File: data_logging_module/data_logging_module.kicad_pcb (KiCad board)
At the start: 2 copper layers, 40 parts, among them U1 PCF8563TS, U2 TLV62569DBV, U3 BME280, Y1 32768Hz

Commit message: Initial scheme
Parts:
- removed D9: D, Diode_SMD:D_PowerDI-123
- added C104: 22u, Capacitor_SMD:C_0805_2012Metric, F.Cu at (205.9, 80.5)
- added C105: 22u, Capacitor_SMD:C_0805_2012Metric, F.Cu at (205.9, 83.5)
- added C301: 100nF, Capacitor_SMD:C_0805_2012Metric, F.Cu at (205.7, 56.0)
- added C302: 100nF, Capacitor_SMD:C_0805_2012Metric, F.Cu at (205.7, 59.0)
- added C303: 100nF, Capacitor_SMD:C_0805_2012Metric, F.Cu at (205.7, 62.1)
- added C304: 100nF, Capacitor_SMD:C_0805_2012Metric, F.Cu at (205.7, 65.1)
- added D201: PESD3V3L1BA,115, Diode_SMD:D_SOD-323, F.Cu at (194.8, 59.0)
- added D202: PESD3V3L1BA,115, Diode_SMD:D_SOD-323, F.Cu at (194.8, 56.0)
- added J1: Conn_01x11, Connector_PinHeader_2.54mm:PinHeader_1x11_P2.54mm_Vertical, F.Cu at (238.6, 57.6)
- added J2: Conn_01x11, Connector_PinHeader_2.54mm:PinHeader_1x11_P2.54mm_Vertical, F.Cu at (243.2, 57.6)
- added R107: 10R, Resistor_SMD:R_0805_2012Metric, F.Cu at (210.3, 80.5)
- added R200: 10kR, Resistor_SMD:R_0805_2012Metric, F.Cu at (194.8, 64.9)
- added R201: 10kR, Resistor_SMD:R_0805_2012Metric, F.Cu at (194.8, 61.9)
- added R301: 4k7R, Resistor_SMD:R_0805_2012Metric, F.Cu at (201.2, 67.8)
- added R302: 4k7R, Resistor_SMD:R_0805_2012Metric, F.Cu at (201.2, 64.9)
- added R303: 4k7R, Resistor_SMD:R_0805_2012Metric, F.Cu at (201.2, 61.9)
- added R304: 5k1R, Resistor_SMD:R_0805_2012Metric, F.Cu at (201.2, 56.0)
- added R305: 5k1R, Resistor_SMD:R_0805_2012Metric, F.Cu at (201.2, 59.0)
- added U101: HT7533-1, Package_TO_SOT_SMD:SOT-89-3, F.Cu at (207.1, 76.0)
- added U301: BME280, Package_LGA:Bosch_LGA-8_2.5x2.5mm_P0.65mm_ClockwisePinNumbering, F.Cu at (205.7, 68.8)
- added U5: DS18B20, Package_TO_SOT_THT:TO-92_Inline, F.Cu at (209.9, 67.5)
- RLO300: renamed from R10; value LDR07 -> LDR
- renumbered C6 to C100, C7 to C101, C8 to C102, C9 to C103, C10 to C106, C4 to C200, C5 to C201, C11 to C300, C2 to C400, C3 to C401, C1 to C402, D10 to D100, D3 to D200, D4 to D203, D5 to D204, D6 to D205, D7 to D206, D1 to D400, D2 to D401, L1 to L100, R7 to R104, R8 to R105, R9 to R106, R3 to R202, R4 to R203, R5 to R204, R6 to R205, R11 to R300, R1 to R400, R2 to R401, U2 to U100, U3 to U300, U1 to U400, Y1 to Y400
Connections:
- net LDR_IN renamed LDR
- net SD_CARD_CS renamed SD_CARD_CS/DAT3
- net SD_CARD_MISO renamed SD_CARD_DAT2
- net SD_CARD_MOSI renamed SD_CARD_DAT1
- net SD_CARD_SCK renamed SD_CARD_DAT0/MISO
- RLO300 pad 2: +3.3V -> +3.3VA
- U300 pad 1: unconnected-(U3-GND-Pad1) -> GND
- U300 pad 2: unconnected-(U3-CSB-Pad2) -> +3.3V
- U300 pad 3: unconnected-(U3-SDI-Pad3) -> I2C_SDA
- U300 pad 4: unconnected-(U3-SCK-Pad4) -> I2C_SCL
- U300 pad 5: unconnected-(U3-SDO-Pad5) -> Net-(U300-SDO)
- U300 pad 6: unconnected-(U3-VDDIO-Pad6) -> +3.3V
- U300 pad 7: unconnected-(U3-GND-Pad7) -> GND
- U300 pad 8: unconnected-(U3-VDD-Pad8) -> +3.3VA

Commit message: BOM updates
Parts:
- added BT400: BC2032-E2, data_logging_module:MPD_BC2032-E2, F.Cu at (237.2, 120.8)
- added J200: 10067847-001RLF, data_logging_module:AMPHENOL_10067847-001RLF, F.Cu at (90.2, 79.5)
- added L101: 15uH, data_logging_module:MWSA0603S, F.Cu at (226.7, 138.3)
- C104, C105: value 22u -> 22uF
- C301, C302, C303, C304: footprint Capacitor_SMD:C_0805_2012Metric -> Capacitor_SMD:C_0603_1608Metric
- moved J1 115.1 mm to (123.5, 58.0)
- moved J2 115.1 mm to (128.2, 58.0)

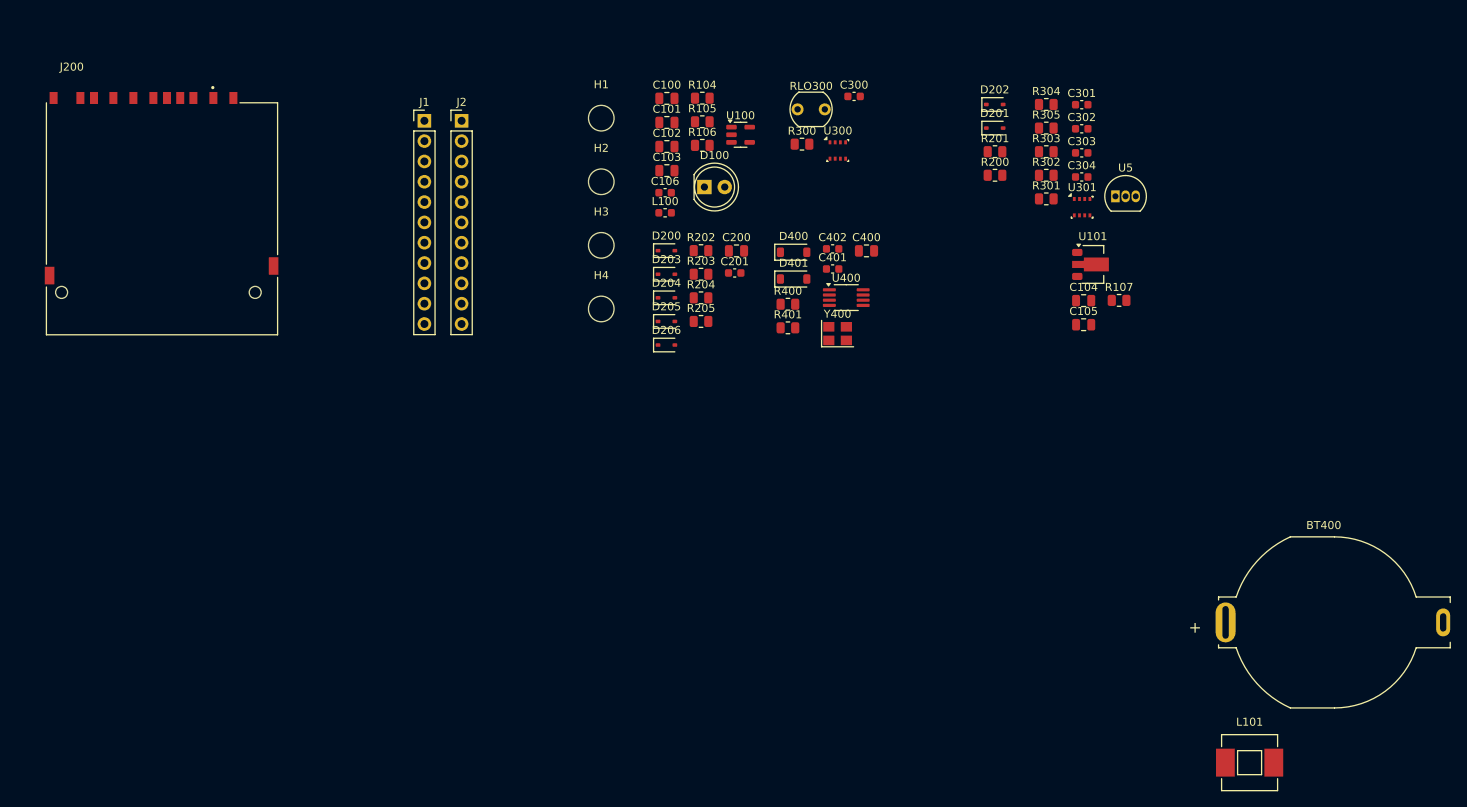
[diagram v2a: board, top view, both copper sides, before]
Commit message: PCB initial layout
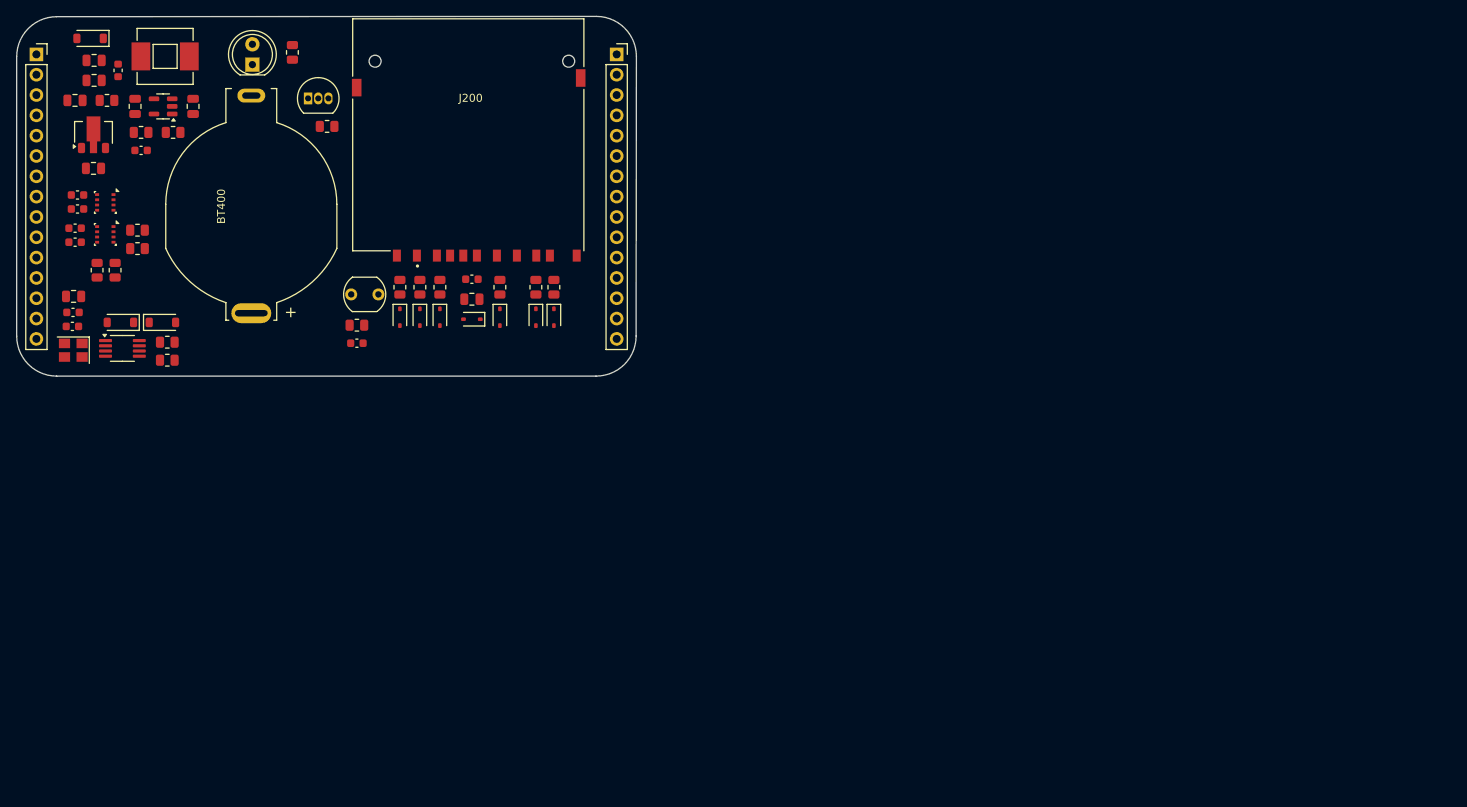
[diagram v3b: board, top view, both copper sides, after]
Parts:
- removed H1, H2, H3, H4: MountingHole, MountingHole:MountingHole_3.2mm_M3
- added D100: 1N4148, Diode_SMD:D_SOD-123, F.Cu at (81.7, 47.8)
- J1, J2: value Conn_01x11 -> Conn_01x15; footprint Connector_PinHeader_2.54mm:PinHeader_1x11_P2.54mm_Vertical -> Connector_PinSocket_2.54mm:PinSocket_1x15_P2.54mm_Vertical
- moved L101 161.8 mm to (91.1, 50.0)
- moved BT400 145.1 mm to (101.9, 68.5), turned to 90 degrees
- moved R107 129.0 mm to (83.8, 55.5)
- moved C104 128.5 mm to (79.8, 55.5), turned to 180 degrees
- moved C301 127.0 mm to (79.8, 73.2), turned to 180 degrees
- moved C302 126.4 mm to (79.8, 71.5), turned to 180 degrees
- moved U101 126.0 mm to (82.1, 59.5), turned to 90 degrees
- moved C303 125.7 mm to (80.1, 69.1), turned to 180 degrees
- moved C304 125.6 mm to (80.1, 67.3), turned to 180 degrees
- moved C105 125.3 mm to (82.1, 64.0), turned to 180 degrees
- moved U301 122.1 mm to (83.6, 68.2), turned to -90 degrees
- moved R305 120.0 mm to (82.6, 76.7), turned to -90 degrees
- moved R304 118.2 mm to (84.8, 76.7), turned to 90 degrees
- moved R303 114.2 mm to (87.6, 74.0), turned to 180 degrees
- moved R302 113.8 mm to (87.6, 71.7), turned to 180 degrees
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- renumbered D100 to D101
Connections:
- J1 pad 10: LDR -> I2C_SCL
- J1 pad 11: DS18B20 -> I2C_SDA
- J1 pad 4: BME280_SCK -> +3.3VA
- J1 pad 5: BME280_SDO -> BME280_SCK
- J1 pad 6: BME280_SDI -> BME280_SDO
- J1 pad 7: BME280_SCB -> BME280_SDI
- J1 pad 8: I2C_SCL -> BME280_SCB
- J1 pad 9: I2C_SDA -> GND
- J2 pad 10: SD_CARD_WP -> SD_CARD_DAT2
- J2 pad 11: SD_CARD_CD -> SD_CARD_CS/DAT3
- J2 pad 2: +3.3VA -> VIN
- J2 pad 3: PCF8563_INT -> +3.3V
- J2 pad 4: SD_CARD_CLK/SCK -> +3.3VA
- J2 pad 5: SD_CARD_CMD/MOSI -> SD_CARD_CLK/SCK
- J2 pad 6: SD_CARD_DAT0/MISO -> SD_CARD_CMD/MOSI
- J2 pad 7: SD_CARD_DAT1 -> GND
- J2 pad 8: SD_CARD_DAT2 -> SD_CARD_DAT0/MISO
- J2 pad 9: SD_CARD_CS/DAT3 -> SD_CARD_DAT1
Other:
- board outline added: 77.5 x 45 mm

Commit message: initial PCB
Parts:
- moved U5 29.7 mm to (115.2, 84.2)
- moved R301 22.2 mm to (117.0, 80.2)
- moved R400 15.1 mm to (79.4, 78.8), turned to 0 degrees
- moved C402 14.5 mm to (93.6, 80.4), turned to 90 degrees
- moved R401 12.9 mm to (79.4, 81.0), turned to 0 degrees
- moved Y400 12.6 mm to (90.7, 80.7), turned to 90 degrees
- moved R106 12.5 mm to (113.0, 60.5), turned to 90 degrees
- moved D101 10.9 mm to (112.0, 55.2), turned to 180 degrees
- moved R302 9.04 mm to (79.3, 75.3), turned to 0 degrees
- moved C302 8.82 mm to (87.2, 76.2), turned to 0 degrees
- moved C300 8.63 mm to (106.5, 84.8), turned to 90 degrees
- moved R303 8.36 mm to (79.3, 73.0), turned to 0 degrees
- moved C304 7.44 mm to (87.2, 69.5), turned to 0 degrees
- moved C303 7.41 mm to (87.2, 67.0), turned to 0 degrees
- moved C301 7.41 mm to (87.2, 73.8), turned to 0 degrees
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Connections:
- J1 pad 13: LDR -> PCF8563_INT
- J1 pad 14: DS18B20 -> LDR
- J1 pad 15: PCF8563_INT -> DS18B20
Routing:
- net +3.3V: track 0.00 -> 263.8 mm, vias 0 -> 5
- net +3.3VA: track 0.00 -> 167.2 mm, vias 0 -> 4
- net VIN: track 0.00 -> 75.9 mm
- net DS18B20: track 0.00 -> 47.2 mm
- net GND: track 0.00 -> 42.3 mm, vias 0 -> 59
- net LDR: track 0.00 -> 42.1 mm
- net SD_CARD_CMD/MOSI: track 0.00 -> 36.8 mm, vias 0 -> 1
- net SD_CARD_DAT2: track 0.00 -> 36.5 mm, vias 0 -> 1
- net SD_CARD_CS/DAT3: track 0.00 -> 34.0 mm, vias 0 -> 1
- net SD_CARD_CLK/SCK: track 0.00 -> 32.7 mm
- net SD_CARD_CD: track 0.00 -> 27.0 mm, vias 0 -> 1
- net I2C_SCL: track 0.00 -> 23.2 mm
- net SD_CARD_DAT0/MISO: track 0.00 -> 21.6 mm
- net SD_CARD_DAT1: track 0.00 -> 18.6 mm
- net BME280_SCK: track 0.00 -> 15.4 mm
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- added copper zone on F.Cu, net +3.3V
- added copper zone on F.Cu, net +5V
- added copper zone on F.Cu, net /[1]Power/+5V_FILT
- added copper zone on F.Cu, net /[1]Power/BUCK_SW
- added copper zone on F.Cu, net GND
- added copper zone on In1.Cu, net GND
- added copper zone on In2.Cu, net GND
- added copper zone on F.Cu, net VIN
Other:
- board size 77.5 x 45 mm -> 77.5 x 40 mm
- copper layers 2 -> 4

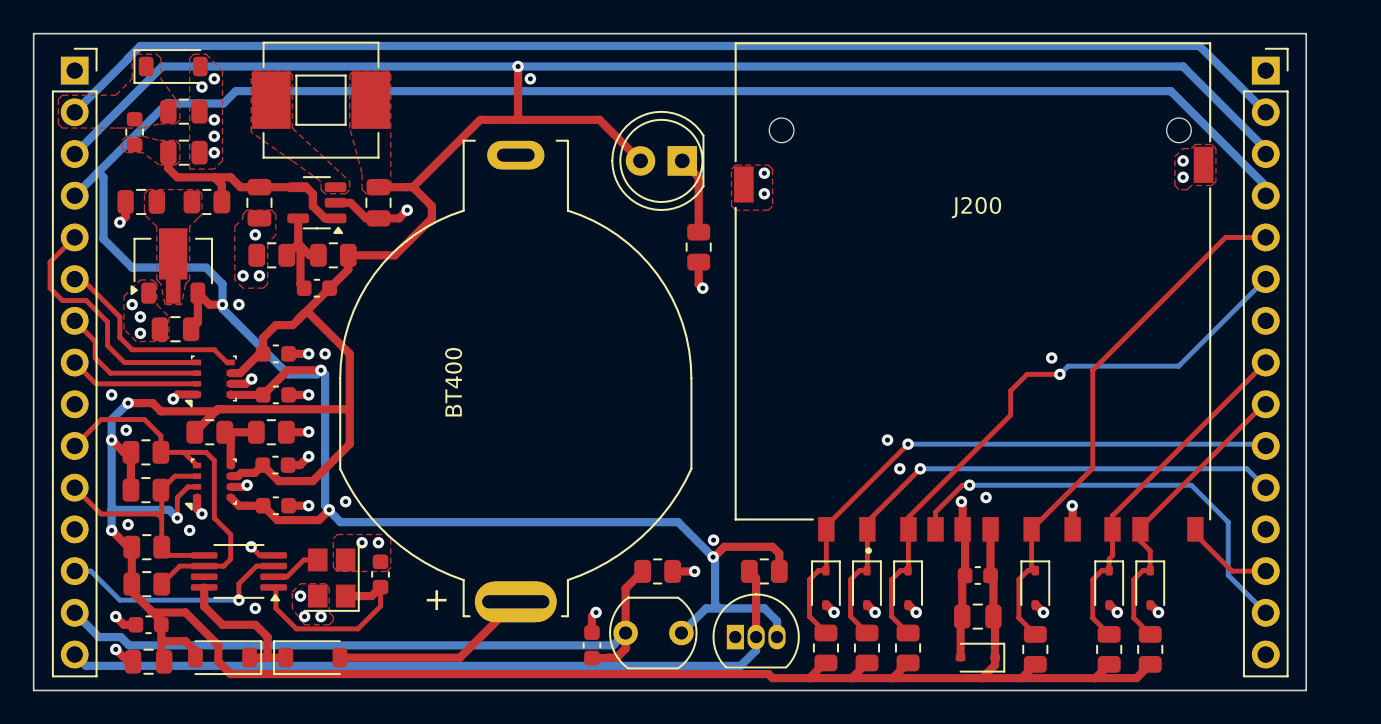
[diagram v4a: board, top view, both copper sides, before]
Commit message: Silkscreen updates
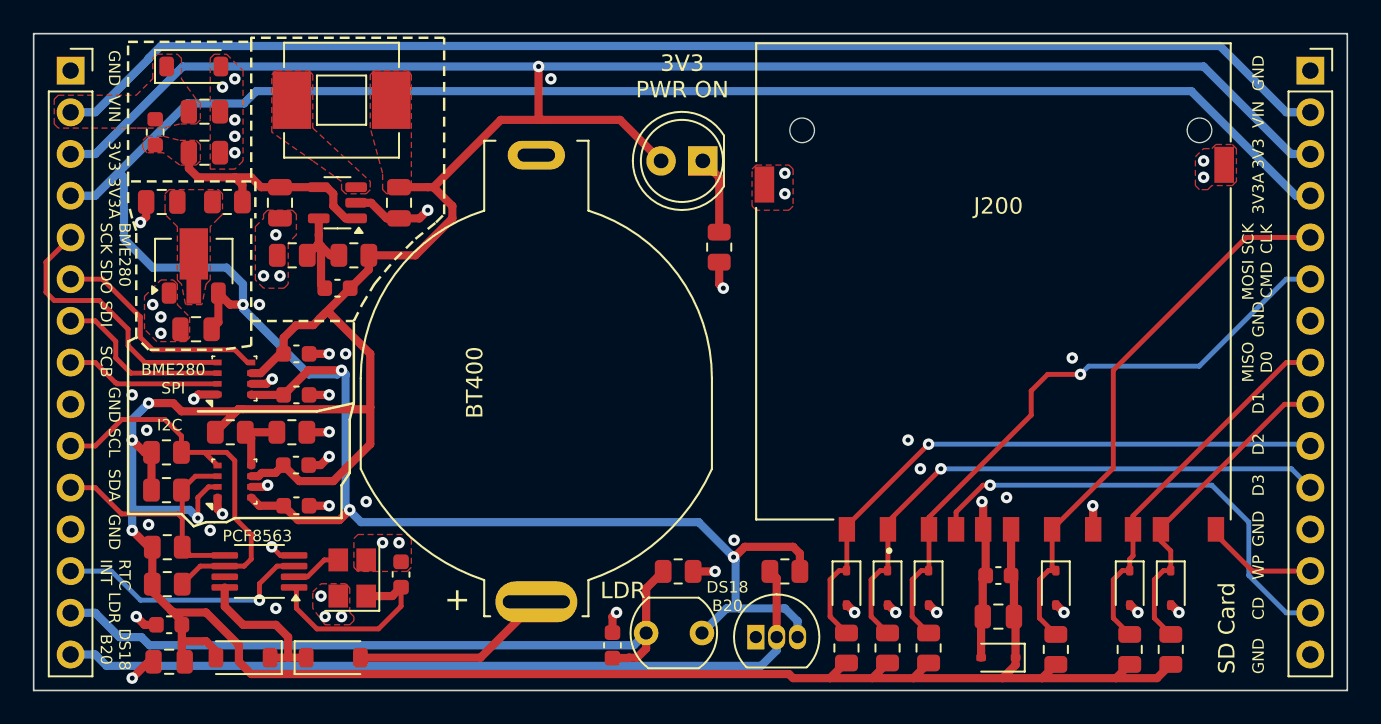
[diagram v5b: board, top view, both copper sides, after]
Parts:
- moved J2 2.71 mm to (150.2, 49.8)
- moved BT400 1.25 mm to (103.1, 68.5)
- moved C100 1.25 mm to (82.9, 52.2)
- moved C101 1.25 mm to (82.9, 54.8)
- moved C102 1.25 mm to (87.5, 57.8)
- moved C103 1.25 mm to (94.8, 57.8)
- moved C104 1.25 mm to (80.3, 57.8)
- moved C105 1.25 mm to (82.4, 65.5)
- moved C106 1.25 mm to (91.0, 63.0)
- moved C200 1.25 mm to (131.2, 83.0)
- moved C201 1.25 mm to (131.2, 80.5)
- moved C300 1.25 mm to (107.8, 84.8)
- moved C301 1.25 mm to (88.5, 73.8)
- moved C302 1.25 mm to (88.5, 76.2)
- moved C303 1.25 mm to (88.5, 67.0)
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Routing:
- net VIN: track 75.9 -> 78.9 mm
- net +3.3V: track 263.8 -> 266.6 mm
- net +3.3VA: track 167.2 -> 169.8 mm
- net PCF8563_INT: track 14.3 -> 15.8 mm
- net LDR: track 42.1 -> 43.6 mm
- net I2C_SDA: track 14.9 -> 16.4 mm
- net I2C_SCL: track 23.2 -> 24.7 mm
- net DS18B20: track 47.2 -> 48.7 mm
- net BME280_SDO: track 12.3 -> 13.8 mm
- net BME280_SDI: track 9.36 -> 10.9 mm
- net BME280_SCB: track 7.99 -> 9.49 mm
- net SD_CARD_WP: track 5.52 -> 6.99 mm
- net SD_CARD_DAT2: track 36.5 -> 38.0 mm
- net SD_CARD_DAT0/MISO: track 21.6 -> 23.1 mm
- net SD_CARD_CS/DAT3: track 34.0 -> 35.4 mm
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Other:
- board size 77.5 x 40 mm -> 80 x 40 mm
- board text added: "3V3"
- board text added: "3V3 PWR ON"
- board text added: "3V3A"
- board text added: "BME280 SCK"
- board text added: "BME280 SPI"
- board text added: "CD"
- board text added: "D1"
- board text added: "D2"
- board text added: "D3"
- board text added: "DS18 B20"
- board text added: "GND"
- board text added: "I2C"
- board text added: "LDR"
- board text added: "MISO D0"
- board text added: "MOSI CMD"
- board text added: "PCF8563"
- board text added: "RTC INT"
- board text added: "SCB"
- board text added: "SCK CLK"
- board text added: "SCL"
- board text added: "SD Card"
- board text added: "SDA"
- board text added: "SDI"
- board text added: "SDO"
- board text added: "VIN"
- board text added: "WP"

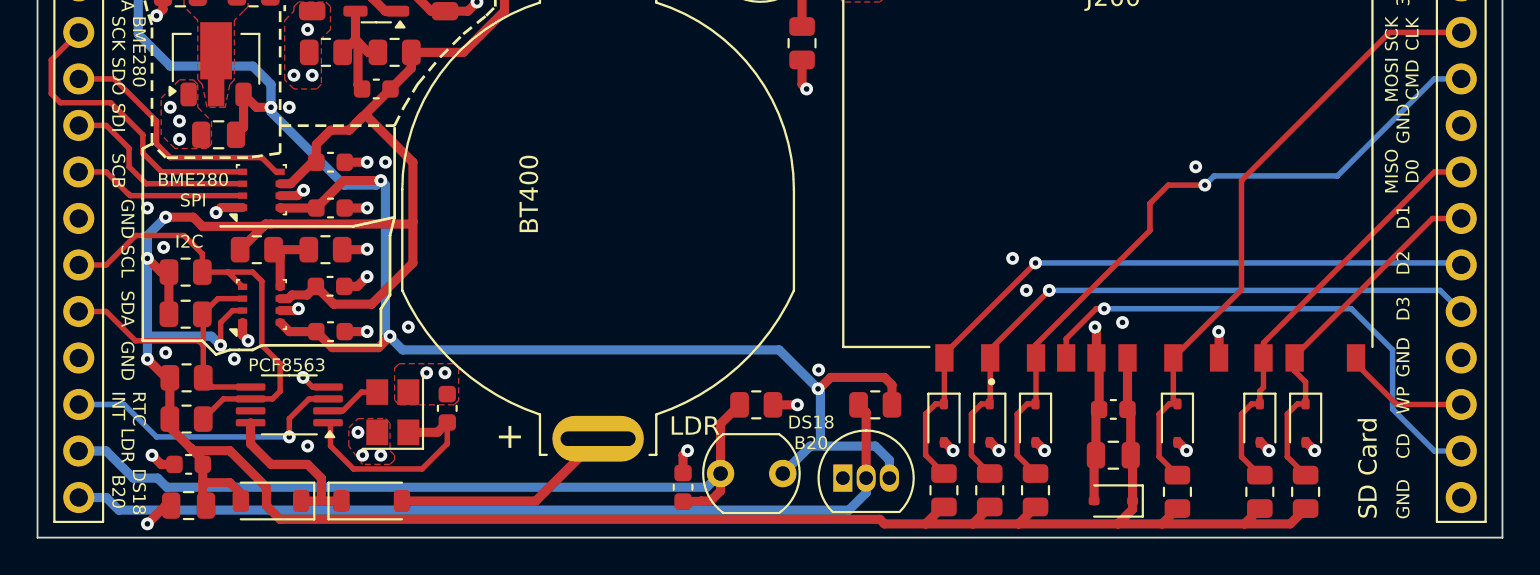
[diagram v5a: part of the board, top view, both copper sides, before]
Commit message: Add scheme plots
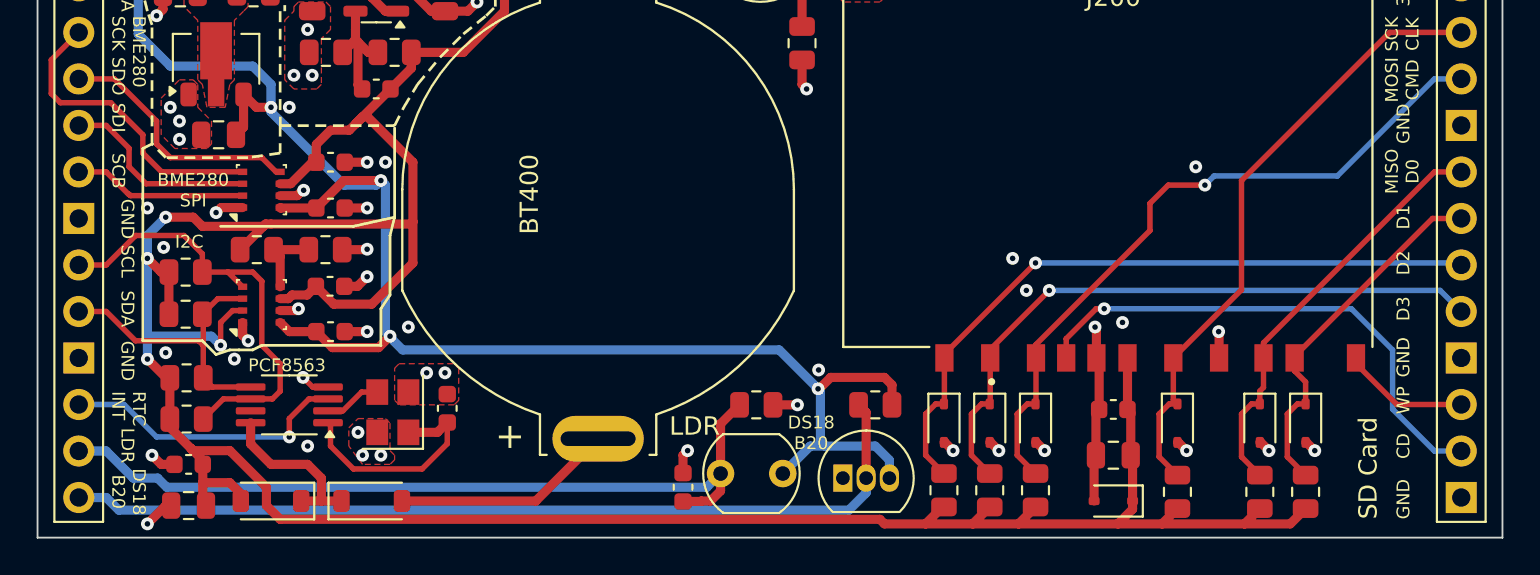
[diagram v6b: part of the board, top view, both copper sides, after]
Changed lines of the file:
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@@
 			(pintype "passive")
 		)
-		(pad "7" thru_hole oval
+		(pad "7" thru_hole rect
 			(at 0 15.24)
 			(size 1.7 1.7)
@@
 			(pintype "passive")
 		)
-		(pad "12" thru_hole oval
+		(pad "12" thru_hole rect
 			(at 0 27.94)
 			(size 1.7 1.7)
@@
 			(pintype "passive")
 		)
-		(pad "15" thru_hole oval
+		(pad "15" thru_hole rect
 			(at 0 35.56)
 			(size 1.7 1.7)
@@
 			(pintype "passive")
 		)
-		(pad "9" thru_hole oval
+		(pad "9" thru_hole rect
 			(at 0 20.32)
 			(size 1.7 1.7)
@@
 			(pintype "passive")
 		)
-		(pad "12" thru_hole oval
+		(pad "12" thru_hole rect
 			(at 0 27.94)
 			(size 1.7 1.7)
@@
 		(polygon
 			(pts
-				(xy 72.5 47.5) (xy 150 47.5) (xy 150 87.5) (xy 72.5 87.5)
+				(xy 72.5 47.5) (xy 152.5 47.5) (xy 152.5 87.5) (xy 72.5 87.5)
 			)
 		)
